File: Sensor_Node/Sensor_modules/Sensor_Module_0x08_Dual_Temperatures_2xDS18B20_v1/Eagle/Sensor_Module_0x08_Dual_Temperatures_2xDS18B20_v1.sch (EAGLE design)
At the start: 18 parts, among them J2 1x3 RA Female .1", J3 1x3 RA Female .1", J4 ARDUINO_ISP, U2 ATMEGA328P_TQFP, Y1 8MHZ

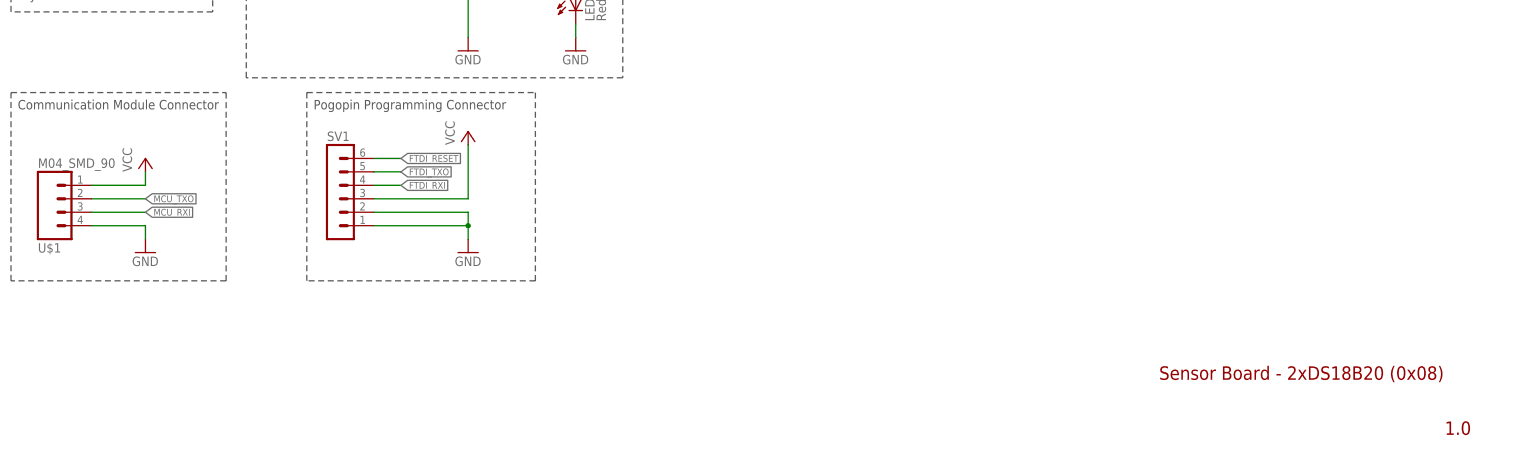
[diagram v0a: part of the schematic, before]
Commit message: Renaming boards to modules inside eagle files
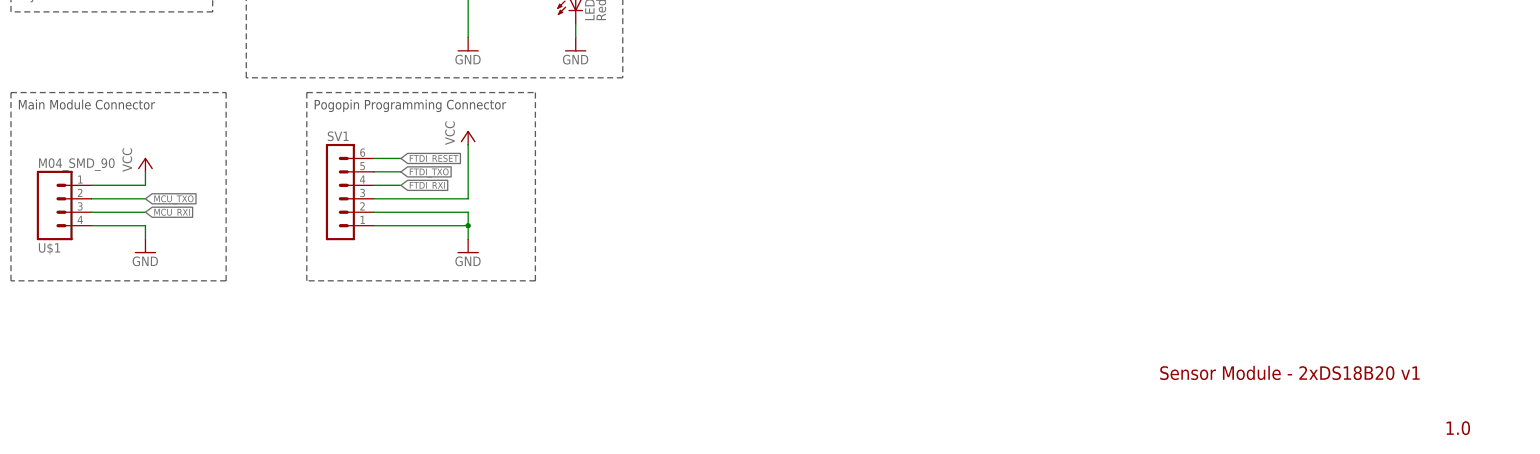
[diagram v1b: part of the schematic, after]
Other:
- note added: "Main Module Connector"
- note added: "Sensor Module - 2xDS18B20 v1"
- note removed: "Communication Module Connector"
- note removed: "Sensor Board - 2xDS18B20 (0x08)"
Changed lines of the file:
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@@
 <?xml version="1.0" encoding="utf-8"?>
 <!DOCTYPE eagle SYSTEM "eagle.dtd">
-<eagle version="8.4.3">
+<eagle version="9.1.1">
 <drawing>
 <settings>
@@
 <wire x1="48.26" y1="65.786" x2="48.26" y2="30.226" width="0.1524" layer="97" style="shortdash"/>
 <wire x1="48.26" y1="30.226" x2="7.62" y2="30.226" width="0.1524" layer="97" style="shortdash"/>
-<text x="8.89" y="62.611" size="1.778" layer="97">Communication Module Connector</text>
+<text x="8.89" y="62.611" size="1.778" layer="97">Main Module Connector</text>
 <wire x1="200.66" y1="152.4" x2="134.62" y2="152.4" width="0.1524" layer="97" style="shortdash"/>
 <wire x1="134.62" y1="88.9" x2="134.62" y2="152.4" width="0.1524" layer="97" style="shortdash"/>
@@
 <wire x1="200.66" y1="88.9" x2="134.62" y2="88.9" width="0.1524" layer="97" style="shortdash"/>
 <text x="137.16" y="147.32" size="1.778" layer="97">DS18B20</text>
-<text x="224.505775" y="11.52471875" size="2.54" layer="94" font="vector">Sensor Board - 2xDS18B20 (0x08)</text>
+<text x="224.505775" y="11.52471875" size="2.54" layer="94" font="vector">Sensor Module - 2xDS18B20 v1</text>
 <text x="278.465165625" y="1.12011875" size="2.54" layer="94" font="vector">1.0</text>
 <wire x1="63.5" y1="30.226" x2="63.5" y2="65.786" width="0.1524" layer="97" style="shortdash"/>
